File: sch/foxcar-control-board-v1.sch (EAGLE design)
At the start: 91 parts, among them Q1 PSMN1R2-30YLC, U1 HMC5883LSMD, U2 SPX29300

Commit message: Info added. Small cleanups.
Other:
- note added: "DIRECTION SERVO"
- note added: "MOTOR DRIVER"
- note added: "POWER"
- note added: "QUADCOPTER ESCs"
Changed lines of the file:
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@@
 <wire x1="0" y1="-27.94" x2="0" y2="59.69" width="0.15" layer="97" style="longdash"/>
 <wire x1="0" y1="59.69" x2="-152.4" y2="59.69" width="0.15" layer="97" style="longdash"/>
-<wire x1="2.54" y1="48.26" x2="2.54" y2="-22.86" width="0.15" layer="97" style="longdash"/>
+<wire x1="2.54" y1="55.88" x2="2.54" y2="-22.86" width="0.15" layer="97" style="longdash"/>
 <wire x1="2.54" y1="-22.86" x2="50.8" y2="-22.86" width="0.15" layer="97" style="longdash"/>
-<wire x1="50.8" y1="-22.86" x2="50.8" y2="48.26" width="0.15" layer="97" style="longdash"/>
-<wire x1="50.8" y1="48.26" x2="2.54" y2="48.26" width="0.15" layer="97" style="longdash"/>
+<wire x1="50.8" y1="-22.86" x2="50.8" y2="55.88" width="0.15" layer="97" style="longdash"/>
+<wire x1="50.8" y1="55.88" x2="2.54" y2="55.88" width="0.15" layer="97" style="longdash"/>
 <wire x1="-7.62" y1="99.06" x2="-7.62" y2="66.04" width="0.15" layer="97" style="longdash"/>
 <wire x1="-7.62" y1="66.04" x2="46.99" y2="66.04" width="0.15" layer="97" style="longdash"/>
@@
 <wire x1="-17.78" y1="104.14" x2="-133.35" y2="104.14" width="0.15" layer="97" style="longdash"/>
 <frame x1="-163.83" y1="-41.91" x2="62.23" y2="116.84" columns="8" rows="5" layer="91"/>
+<text x="-130.81" y="99.06" size="2.1844" layer="97">POWER</text>
+<text x="-149.86" y="54.61" size="2.1844" layer="97">MOTOR DRIVER</text>
+<text x="-5.08" y="90.17" size="2.1844" layer="97">DIRECTION
+SERVO</text>
+<text x="5.08" y="46.99" size="2.1844" layer="97">QUADCOPTER
+ESCs</text>
 </plain>
 <instances>
@@
 <sheet>
 <plain>
-<text x="153.67" y="261.62" size="1.778" layer="97">MAGNETOMETER</text>
-<text x="73.66" y="261.62" size="1.778" layer="97">ACCEL/GYRO</text>
-<wire x1="15.24" y1="270.51" x2="15.24" y2="209.55" width="0.15" layer="97" style="longdash"/>
-<wire x1="15.24" y1="209.55" x2="219.71" y2="209.55" width="0.15" layer="97" style="longdash"/>
-<wire x1="219.71" y1="209.55" x2="219.71" y2="270.51" width="0.15" layer="97" style="longdash"/>
-<wire x1="219.71" y1="270.51" x2="15.24" y2="270.51" width="0.15" layer="97" style="longdash"/>
+<text x="17.78" y="265.43" size="2.1844" layer="97">ACCEL/GYRO</text>
+<wire x1="15.24" y1="270.51" x2="15.24" y2="208.28" width="0.15" layer="97" style="longdash"/>
+<wire x1="15.24" y1="208.28" x2="120.65" y2="208.28" width="0.15" layer="97" style="longdash"/>
+<wire x1="120.65" y1="208.28" x2="120.65" y2="270.51" width="0.15" layer="97" style="longdash"/>
+<wire x1="120.65" y1="270.51" x2="15.24" y2="270.51" width="0.15" layer="97" style="longdash"/>
 <frame x1="7.62" y1="5.08" x2="396.24" y2="280.67" columns="8" rows="5" layer="97"/>
 <wire x1="289.56" y1="125.73" x2="299.72" y2="125.73" width="0.15" layer="93"/>
+<text x="134.62" y="265.43" size="2.1844" layer="97">MAGNETOMETER</text>
+<wire x1="128.27" y1="208.28" x2="128.27" y2="270.51" width="0.15" layer="97" style="longdash"/>
+<wire x1="128.27" y1="270.51" x2="218.44" y2="270.51" width="0.005" layer="97" style="longdash"/>
+<wire x1="218.44" y1="270.51" x2="218.44" y2="208.28" width="0.005" layer="97" style="longdash"/>
+<wire x1="218.44" y1="208.28" x2="128.27" y2="208.28" width="0.005" layer="97" style="longdash"/>
 </plain>
 <instances>
@@
 <segment>
 <pinref part="U$10" gate="G$1" pin="PB12"/>
-<wire x1="199.39" y1="77.47" x2="193.04" y2="77.47" width="0.15" layer="91"/>
-<label x="193.04" y="77.47" size="1.778" layer="95" rot="R180" xref="yes"/>
+<wire x1="199.39" y1="77.47" x2="196.85" y2="77.47" width="0.15" layer="91"/>
+<wire x1="196.85" y1="77.47" x2="191.77" y2="81.28" width="0.15" layer="91"/>
+<label x="191.77" y="81.28" size="1.778" layer="95" rot="R180" xref="yes"/>
 </segment>
 <segment>
@@
 <segment>
 <pinref part="U$10" gate="G$1" pin="PB13"/>
-<wire x1="199.39" y1="74.93" x2="193.04" y2="74.93" width="0.15" layer="91"/>
-<label x="193.04" y="74.93" size="1.778" layer="95" rot="R180" xref="yes"/>
+<wire x1="199.39" y1="74.93" x2="196.85" y2="74.93" width="0.15" layer="91"/>
+<wire x1="196.85" y1="74.93" x2="191.77" y2="77.47" width="0.15" layer="91"/>
+<label x="191.77" y="77.47" size="1.778" layer="95" rot="R180" xref="yes"/>
 </segment>
 <segment>
@@
 <segment>
 <pinref part="U$10" gate="G$1" pin="PB14"/>
-<wire x1="199.39" y1="72.39" x2="193.04" y2="72.39" width="0.15" layer="91"/>
-<label x="193.04" y="72.39" size="1.778" layer="95" rot="R180" xref="yes"/>
+<wire x1="199.39" y1="72.39" x2="196.85" y2="72.39" width="0.15" layer="91"/>
+<wire x1="196.85" y1="72.39" x2="191.77" y2="73.66" width="0.15" layer="91"/>
+<label x="191.77" y="73.66" size="1.778" layer="95" rot="R180" xref="yes"/>
 </segment>
 <segment>
@@
 <segment>
 <pinref part="U$10" gate="G$1" pin="PB15"/>
-<wire x1="199.39" y1="69.85" x2="193.04" y2="69.85" width="0.15" layer="91"/>
-<label x="193.04" y="69.85" size="1.778" layer="95" rot="R180" xref="yes"/>
+<wire x1="199.39" y1="69.85" x2="191.77" y2="69.85" width="0.15" layer="91"/>
+<label x="191.77" y="69.85" size="1.778" layer="95" rot="R180" xref="yes"/>
 </segment>
 <segment>
@@
 <segment>
 <pinref part="U$10" gate="G$1" pin="PB10"/>
-<wire x1="199.39" y1="90.17" x2="187.96" y2="90.17" width="0.15" layer="91"/>
+<wire x1="199.39" y1="90.17" x2="173.99" y2="90.17" width="0.15" layer="91"/>
 <label x="190.5" y="90.17" size="1.778" layer="95"/>
-<wire x1="187.96" y1="90.17" x2="180.34" y2="82.55" width="0.15" layer="91"/>
+<wire x1="173.99" y1="90.17" x2="166.37" y2="82.55" width="0.15" layer="91"/>
 <pinref part="JP13" gate="G$1" pin="3"/>
 <label x="156.21" y="82.55" size="1.778" layer="95"/>
-<wire x1="180.34" y1="82.55" x2="154.94" y2="82.55" width="0.15" layer="91"/>
+<wire x1="166.37" y1="82.55" x2="154.94" y2="82.55" width="0.15" layer="91"/>
 </segment>
 </net>
@@
 <pinref part="JP13" gate="G$1" pin="2"/>
 <label x="156.21" y="80.01" size="1.778" layer="95"/>
-<wire x1="154.94" y1="80.01" x2="180.34" y2="80.01" width="0.15" layer="91"/>
-<wire x1="180.34" y1="80.01" x2="187.96" y2="87.63" width="0.15" layer="91"/>
+<wire x1="154.94" y1="80.01" x2="166.37" y2="80.01" width="0.15" layer="91"/>
+<wire x1="166.37" y1="80.01" x2="173.99" y2="87.63" width="0.15" layer="91"/>
 <pinref part="U$10" gate="G$1" pin="PB11"/>
-<wire x1="199.39" y1="87.63" x2="187.96" y2="87.63" width="0.15" layer="91"/>
+<wire x1="199.39" y1="87.63" x2="173.99" y2="87.63" width="0.15" layer="91"/>
 <label x="190.5" y="87.63" size="1.778" layer="95"/>
 </segment>
@@
 </schematic>
 </drawing>
+<compatibility>
+<note version="6.3" minversion="6.2.2" severity="warning">
+Since Version 6.2.2 text objects can contain more than one line,
+which will not be processed correctly with this version.
+</note>
+</compatibility>
 </eagle>

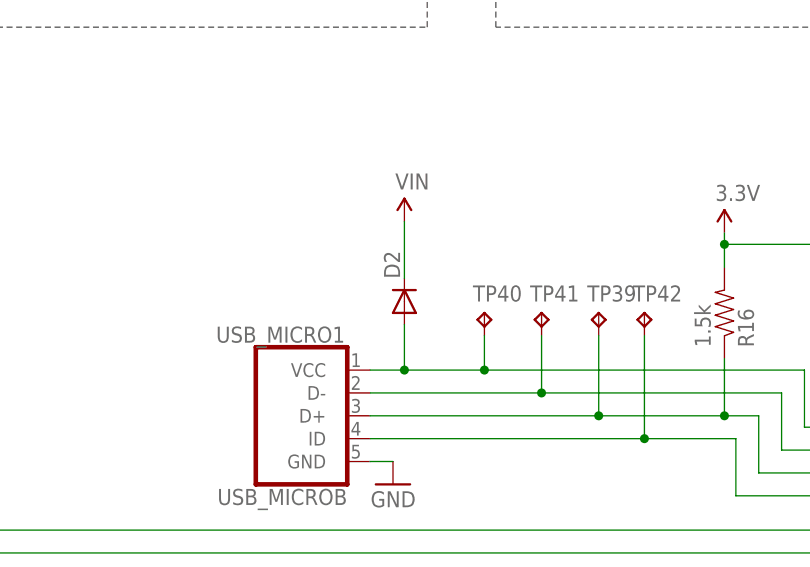
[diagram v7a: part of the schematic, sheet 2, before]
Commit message: The last of the ERCs. Chose diode and LEDs.
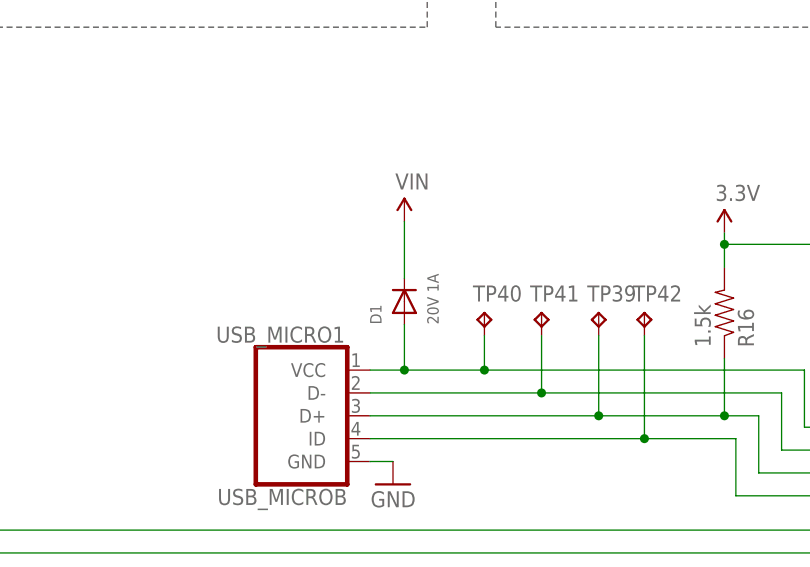
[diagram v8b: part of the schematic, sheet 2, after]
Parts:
- removed D2: (no value), SparkFun-DiscreteSemi:DIODESMA-ALT
- added D1: 20V 1A, adafruit:DIODESMA
- LED3, LED4: value (none) -> GREEN
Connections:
- net FS_VBUS: now also D1.A; no longer D2.A
- net VIN: now also D1.C; no longer D2.C
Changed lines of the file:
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@@
 <part name="DIG_GND11" library="SparkFun-Aesthetics" deviceset="GND" device="" value="GND"/>
 <part name="R16" library="SparkFun-Passives" deviceset="RESISTOR" device="0402-RES" value="1.5k"/>
-<part name="D2" library="SparkFun-DiscreteSemi" deviceset="DIODE" device="SMA-ALT"/>
 <part name="TP39" library="testpad" deviceset="TP" device="TP06R"/>
 <part name="TP40" library="testpad" deviceset="TP" device="TP06R"/>
@@
 <part name="C15" library="rcl3" deviceset="C-EU" device="C0603" value="0.33uF"/>
 <part name="U$12" library="SparkFun-Aesthetics" deviceset="VIN" device=""/>
-<part name="LED3" library="led" deviceset="LED" device="CHIP-LED0603"/>
-<part name="LED4" library="led" deviceset="LED" device="CHIP-LED0603"/>
+<part name="LED3" library="led" deviceset="LED" device="CHIP-LED0603" value="GREEN"/>
+<part name="LED4" library="led" deviceset="LED" device="CHIP-LED0603" value="GREEN"/>
 <part name="R1" library="SparkFun-Passives" deviceset="RESISTOR" device="0402-RES" value="270"/>
 <part name="R3" library="SparkFun-Passives" deviceset="RESISTOR" device="0402-RES" value="50"/>
@@
 <part name="JP7" library="SparkFun-Connectors" deviceset="M10" device="LOCK_LONGPADS" value=""/>
 <part name="JP9" library="SparkFun-Connectors" deviceset="M10" device="LOCK_LONGPADS" value=""/>
+<part name="D1" library="adafruit" deviceset="DIODE" device="SMA" value="20V 1A"/>
 </parts>
 <sheets>
@@
 <instance part="DIG_GND11" gate="1" x="116.84" y="157.48" rot="MR0"/>
 <instance part="R16" gate="G$1" x="153.67" y="176.53" rot="MR90"/>
-<instance part="D2" gate="G$1" x="118.11" y="177.8" rot="R90"/>
 <instance part="TP39" gate="G$1" x="139.7" y="176.53"/>
 <instance part="TP40" gate="G$1" x="127" y="176.53"/>
@@
 <instance part="JP7" gate="G$1" x="328.93" y="78.74" rot="R180"/>
 <instance part="JP9" gate="G$1" x="316.23" y="50.8" rot="R180"/>
+<instance part="D1" gate="G$1" x="118.11" y="177.8" rot="R90"/>
 </instances>
 <busses>
@@
 <wire x1="114.3" y1="170.18" x2="118.11" y2="170.18" width="0.15" layer="91"/>
 <wire x1="118.11" y1="170.18" x2="118.11" y2="175.26" width="0.15" layer="91"/>
-<pinref part="D2" gate="G$1" pin="A"/>
 <wire x1="118.11" y1="170.18" x2="127" y2="170.18" width="0.15" layer="91"/>
 <pinref part="TP40" gate="G$1" pin="TP"/>
@@
 <label x="177.8" y="163.83" size="1.778" layer="95"/>
 <pinref part="U$10" gate="G$1" pin="PA9"/>
+<pinref part="D1" gate="G$1" pin="A"/>
 </segment>
 </net>
@@
 <net name="VIN" class="0">
 <segment>
-<pinref part="D2" gate="G$1" pin="C"/>
 <wire x1="118.11" y1="180.34" x2="118.11" y2="186.69" width="0.15" layer="91"/>
 <pinref part="U$2" gate="G$1" pin="VIN"/>
-</segment>
-</net>
+<pinref part="D1" gate="G$1" pin="C"/>
+</segment>
+</net>
